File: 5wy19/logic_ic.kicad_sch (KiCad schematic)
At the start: 10 parts, among them IC9 0504TAK, Q28 BCR183, U2 74HC32

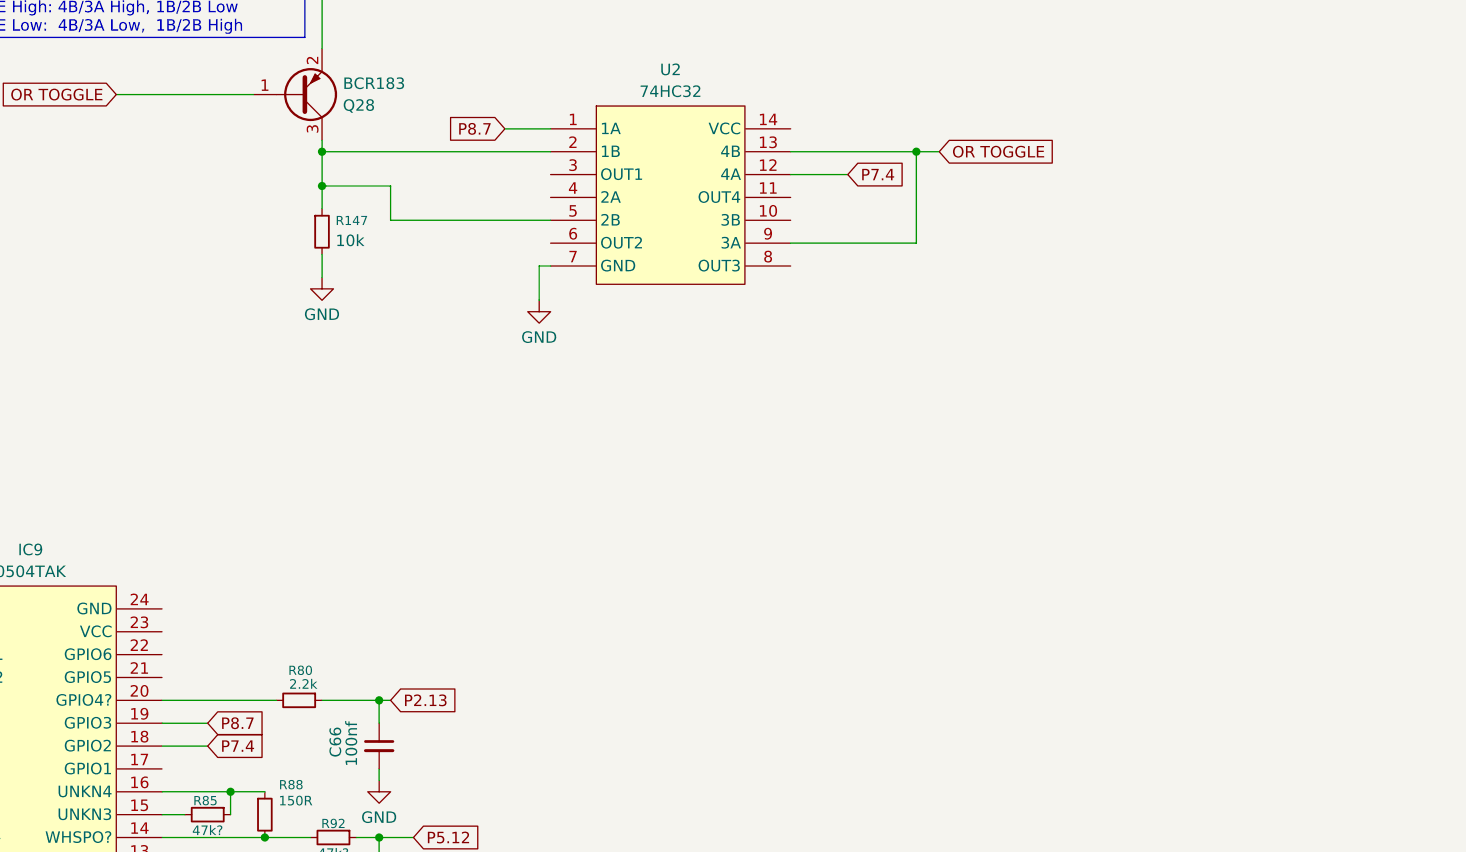
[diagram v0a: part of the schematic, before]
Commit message: Mapped out more pins of MCU and relevant circuits
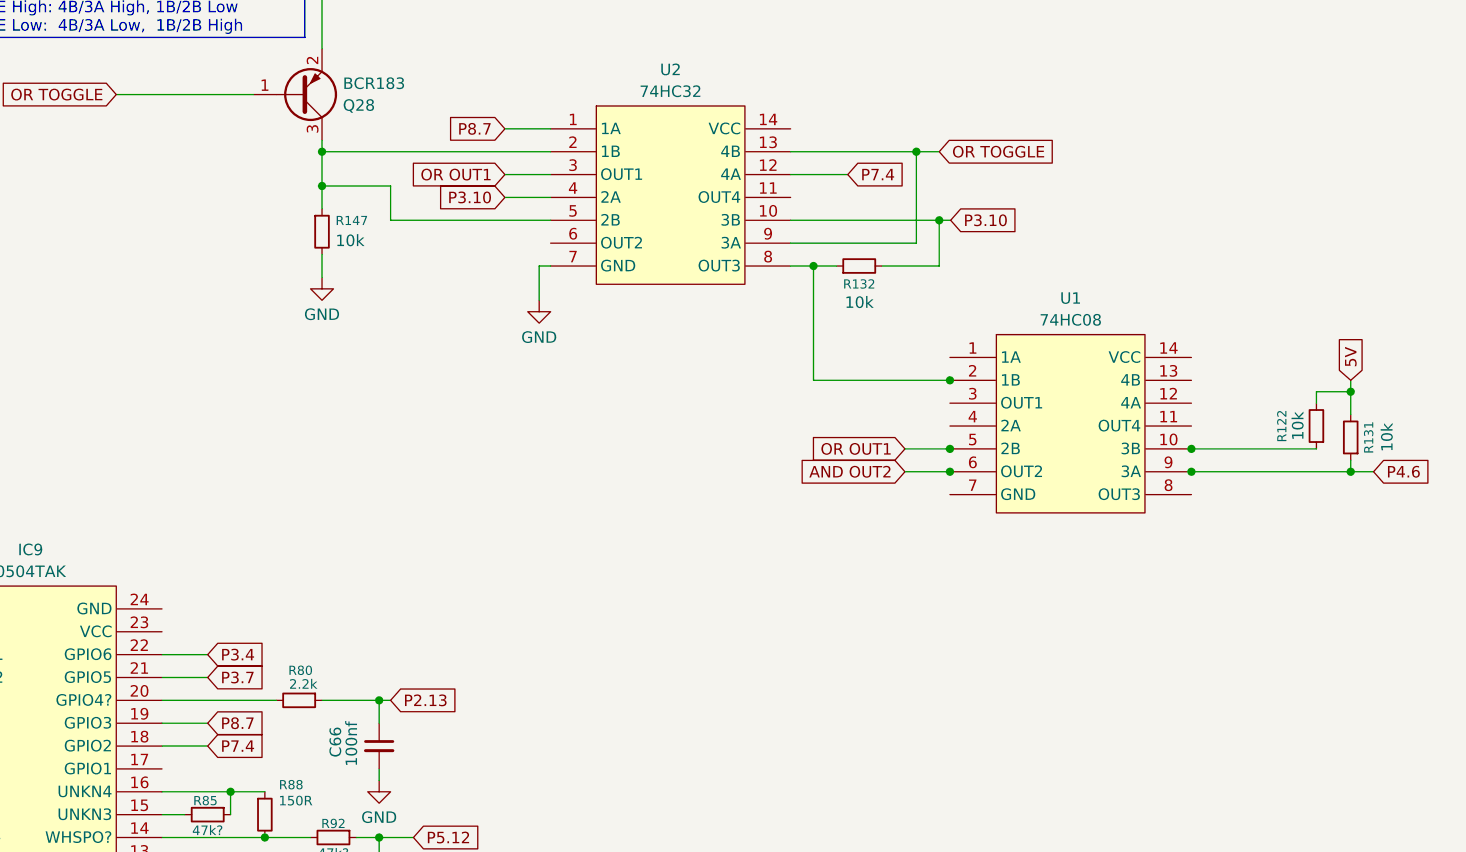
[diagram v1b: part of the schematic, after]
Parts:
- added R122, R131, R132: 10k, symbol Device:R_Small
- added U1: 74HC08, symbol SIMK43:74HC08
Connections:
- net 5V: now also R122.2, R131.2
- net P3.7: now reaches IC9.21 (GPIO5)
- net P3.4: now reaches IC9.22 (GPIO6)
- net P3.10: now reaches U2.10 (3B)
- net P3.10: now also U2.4 (2A), R132.2
- net OR OUT1: now reaches U2.3 (OUT1)
- net OR OUT1: now also U1.5 (2B)
- net at U2.8 (OUT3): now also R132.1, U1.2 (1B)
- new net: R122.1, U1.10 (3B)
- new net AND OUT2: U1.6 (OUT2)
- new net P4.6: R131.1, U1.9 (3A)

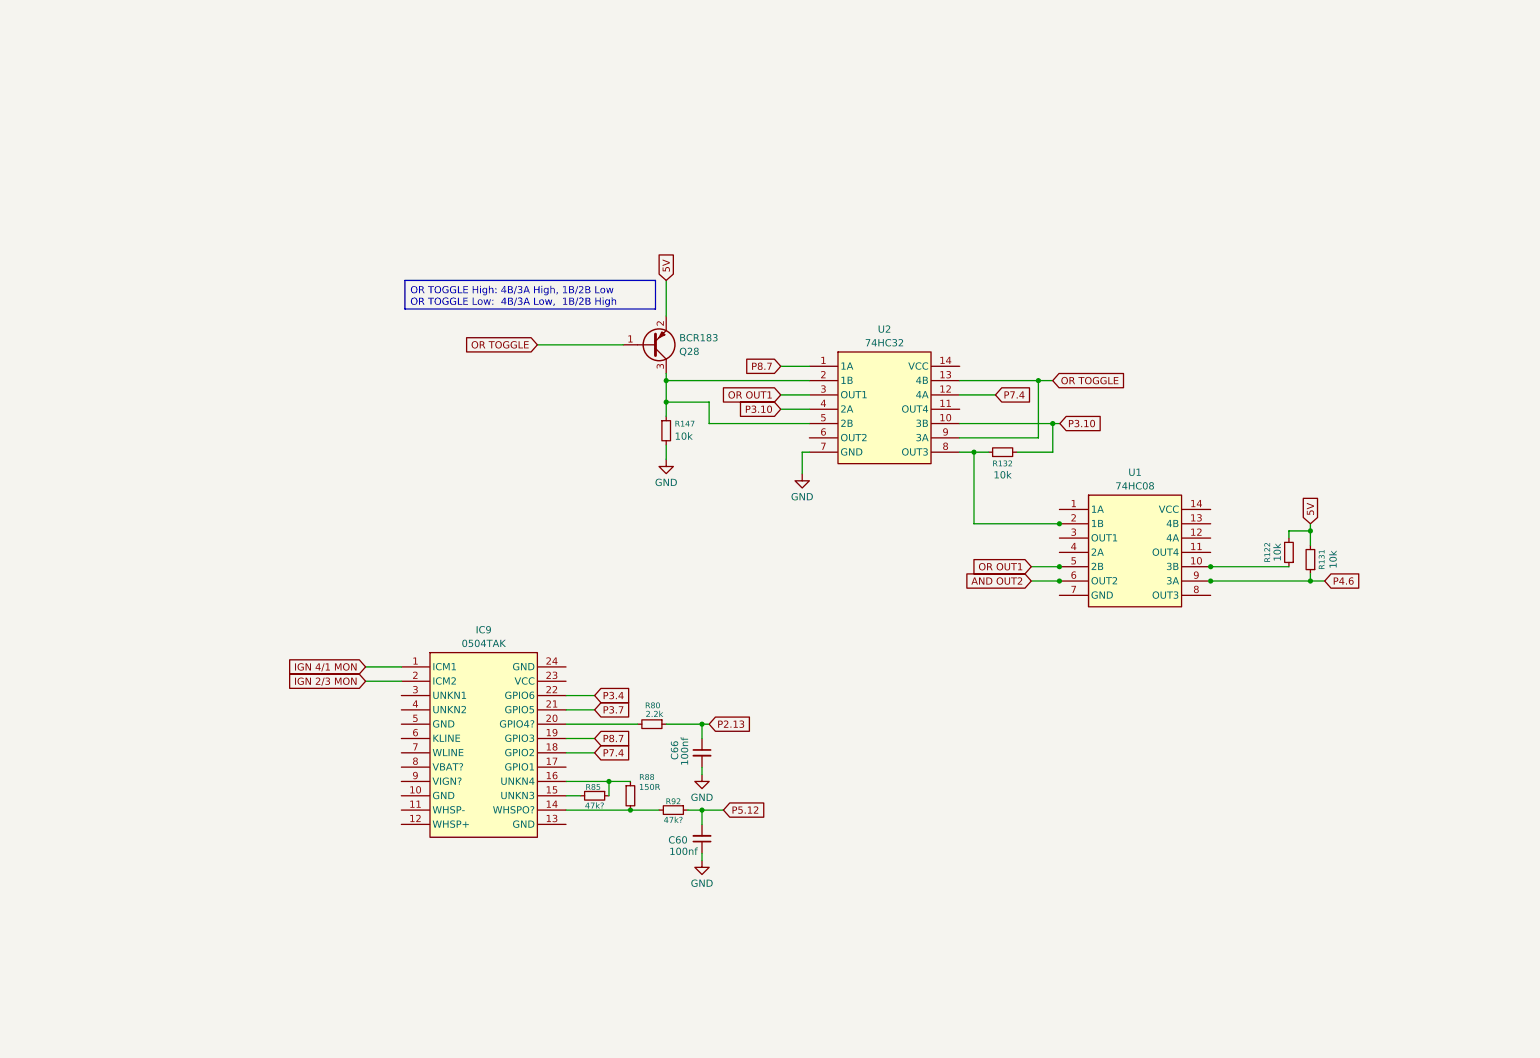
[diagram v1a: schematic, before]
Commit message: Finished most of the subsystems
-- MCU finished
-- Flash finished
-- Power Supply finished
-- I/O Drivers finished
-- CANBUS finished
-- Knock Control finished
-- Connector finished
-- Ignition Driver finished
-- Sensor Logic mostly finished
-- Logic ICs need some work
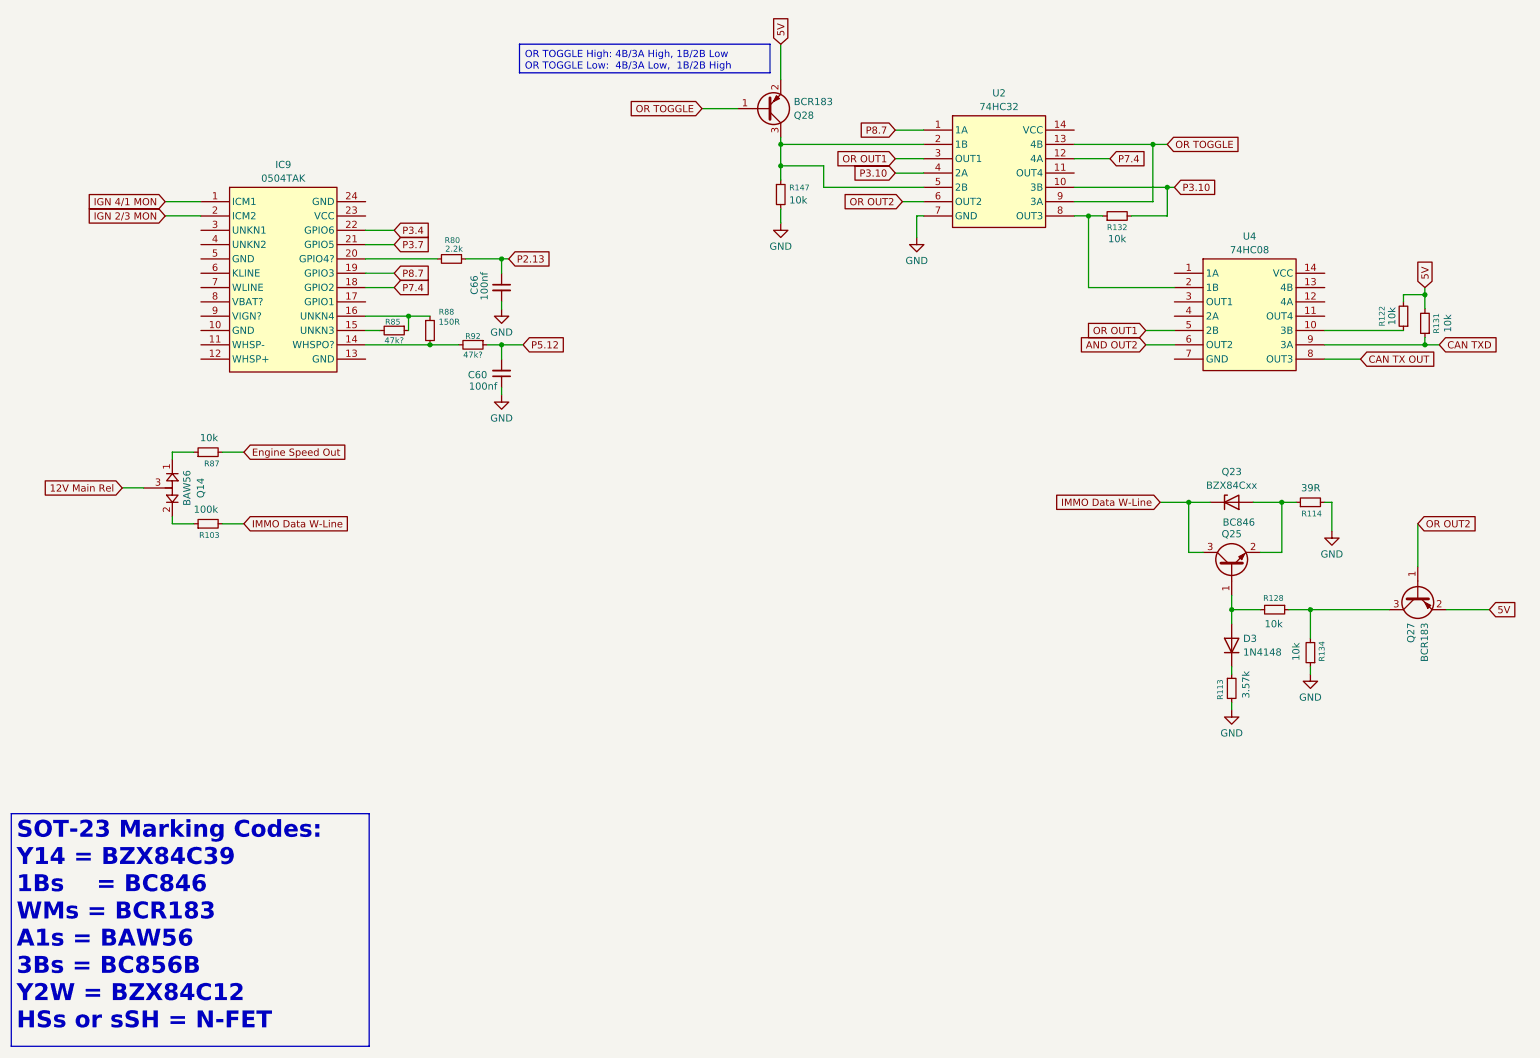
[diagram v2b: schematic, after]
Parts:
- removed U1: 74HC08, symbol SIMK43:74HC08
- added D3: 1N4148, Diode_THT:D_DO-35_SOD27_P7.62mm_Horizontal, symbol Diode:1N4148
- added Q14: BAW56, symbol SIMK43:BAW56
- added Q23: BZX84Cxx, Package_TO_SOT_SMD:SOT-23, symbol Diode:BZX84Cxx
- added Q25: BC846, Package_TO_SOT_SMD:SOT-23, symbol Transistor_BJT:BC846
- added Q27: BCR183, Package_TO_SOT_SMD:SOT-23, symbol Transistor_BJT:BC807
- added R103: 100k, symbol Device:R_Small
- added R113: 3.57k, symbol Device:R_Small
- added R114: 39R, symbol Device:R_Small
- added R128, R134, R87: 10k, symbol Device:R_Small
- added U4: 74HC08, symbol SIMK43:74HC08
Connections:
- net 5V: now also Q27.2 (E)
- net AND OUT2: now also U4.6 (OUT2)
- net GND: now also R113.2, R114.2, R134.1
- net OR OUT1: now also U4.5 (2B)
- net at R122.1: now also U4.10 (3B)
- net at R132.1, U2.8 (OUT3): now also U4.2 (1B)
- net OR OUT2: now reaches U2.6 (OUT2)
- net OR OUT2: now also Q27.1 (B)
- net P4.6 renamed CAN TXD
- net CAN TXD: now also U4.9 (3A)
- new net: D3.1 (K), R113.1
- new net: Q14.1, R87.1
- new net: Q27.3 (C), R128.1, R134.2
- new net: D3.2 (A), Q25.1 (B), R128.2
- new net: Q23.1 (A), Q25.2 (E), R114.1
- new net: Q14.2, R103.1
- new net 12V Main Rel: Q14.3
- new net CAN TX OUT: U4.8 (OUT3)
- new net Engine Speed Out: R87.2
- new net IMMO Data W-Line: Q23.3 (K), Q25.3 (C), R103.2
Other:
- title: (none) -> SMIK43 5WY19 Rev. Eng
- moved on the sheet: C60, C66, IC9, Q28, R122, R131, R132, R147, R80, R85, R88, R92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

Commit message: Final schematic (except maybe some oversights)
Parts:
- added C31, C70, C71, C74: 100nf, symbol Device:C_Small
- added Q26: BAW56, symbol SIMK43:BAW56
- added R118, R63, R67: 10k, symbol Device:R_Small
- added R130: 100k, symbol Device:R_Small
- added R138: 2k, symbol Device:R_Small
- added R71: 22.1k, symbol Device:R_Small
- added R79: 31.6k, symbol Device:R_Small
- IC9: value 0504TAK -> ATM46C3
- renumbered D3 to D11, U4 to U1
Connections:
- net 12V Main Rel: now also R79.1
- net 5V: now also IC9.23 (VCC), U1.14 (VCC), U2.14 (VCC), C31.1, C70.1, C71.1, R118.2, R63.1, R67.1, R71.1
- net GND: now also IC9.10 (GND), IC9.13 (GND), IC9.24 (GND), IC9.5 (GND), U1.7 (GND), C31.2, C70.2, C71.2, C74.2
- net IMMO Data W-Line: now also IC9.7 (WLINE)
- net at R87.1: now also Q14.2; no longer Q14.1
- net at R103.1: now also Q14.1; no longer Q14.2
- net WHSP IN-: now reaches IC9.11 (WHSP-)
- net WHSP IN+: now reaches IC9.12 (WHSP+)
- net TxD Out: now reaches IC9.17 (GPIO1)
- net TxD Out: now also U1.3 (OUT1)
- net at IC9.3 (UNKN1): now also R63.2
- net at IC9.4 (UNKN2): now also R67.2
- net K-Line: now reaches IC9.6 (KLINE)
- net K-Line: now also R130.2
- net ATM46 PIN8: now reaches IC9.8 (VBAT?)
- net ATM46 PIN8: now also R71.2, R79.2
- net ATM46 PIN9: now reaches IC9.9 (VIGN?)
- net ATM46 PIN9: now also R138.1
- net OR OUT4: now reaches U2.11 (OUT4)
- net OR OUT4: now also U1.4 (2A)
- net at U1.1 (1A): now also R118.1
- net AND OUT2 renamed RxD
- net OR OUT2 renamed TxD W-Line
- net P3.10 renamed TxD
- net P7.4 renamed RxD Out 2
- net P8.7 renamed RxD Out 1
- new net: C74.1, Q26.2, R138.2
- new net: Q26.1, R130.1
- new net 12V Ign: Q26.3
- no-connect marks 0 -> 3
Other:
- moved on the sheet: C60, C66, D11, IC9, Q14, Q23, Q25, Q27, Q28, R103, R113, R114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
